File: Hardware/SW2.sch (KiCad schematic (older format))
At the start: 6 parts, among them SW2 SW_Rotary2x4

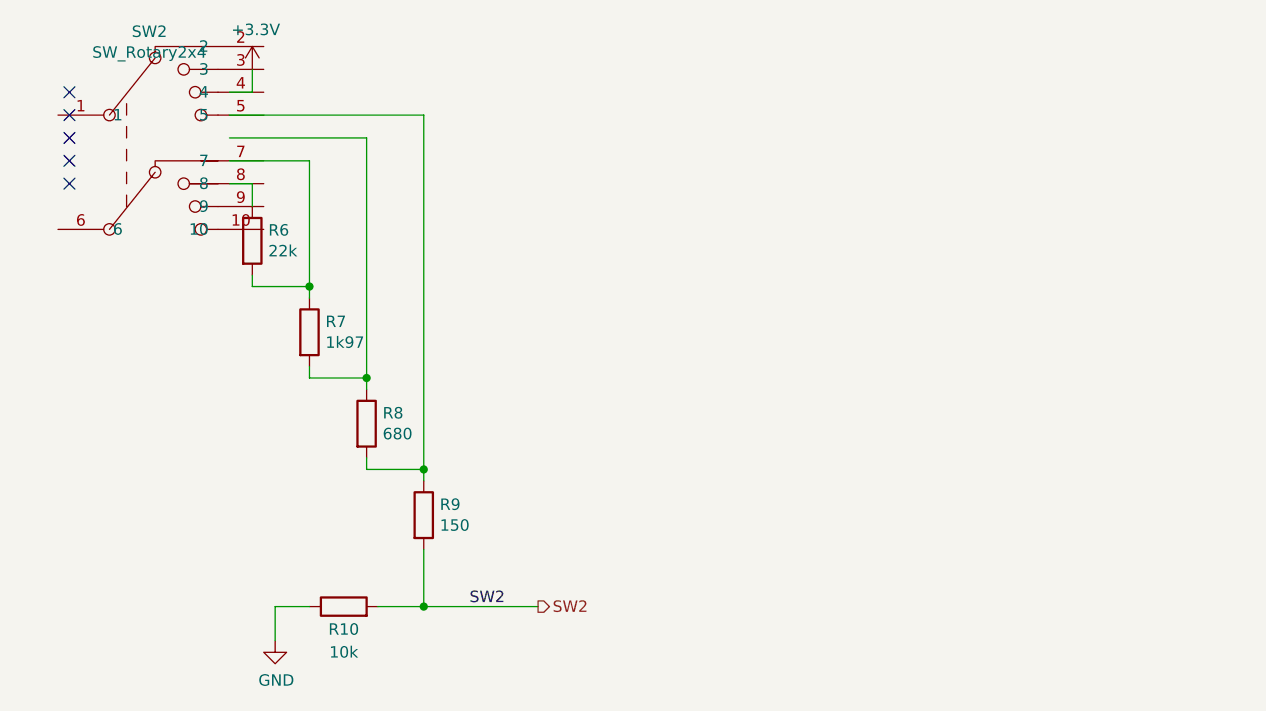
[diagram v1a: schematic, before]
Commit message: symbol changed, bigger cable hole in the middle
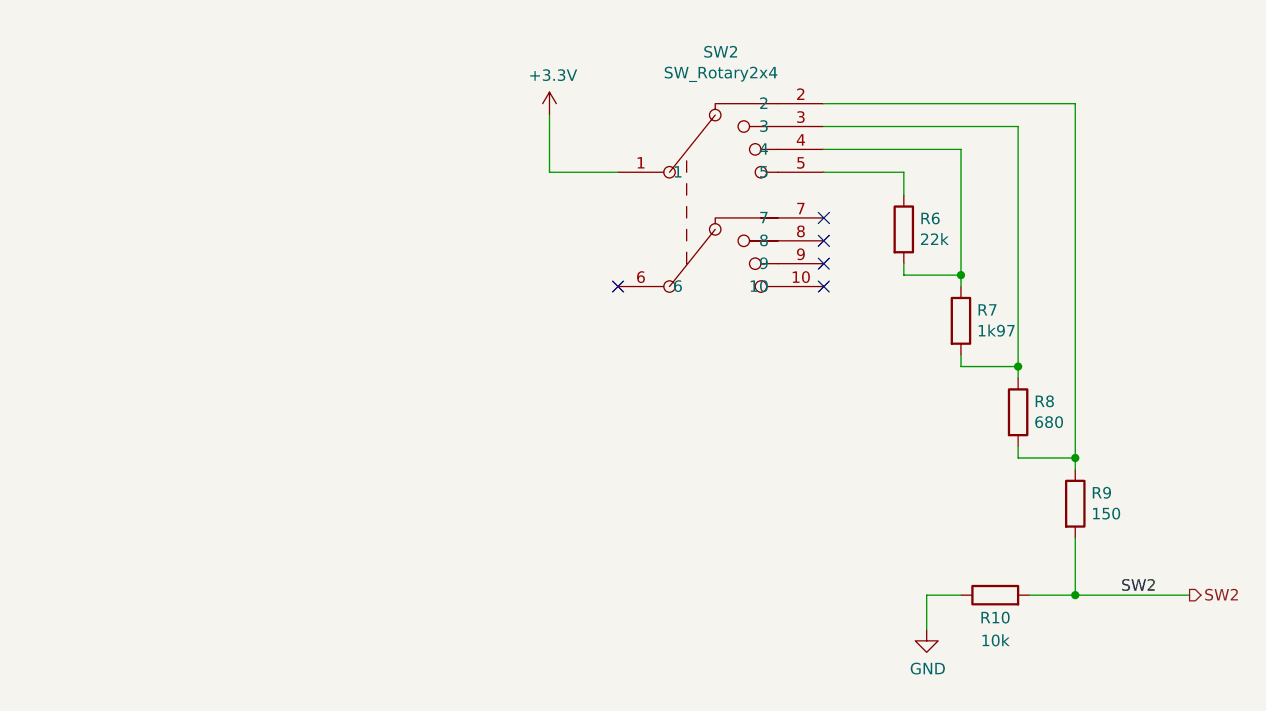
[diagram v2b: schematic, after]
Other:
- moved on the sheet: R10, R6, R7, R8, R9
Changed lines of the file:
@@
 $EndDescr
-$Comp
-L Switch:SW_Rotary2x4 SW?
-U 1 1 61B9B255
-P 4350 2700
-AR Path="/61B7E6EB/61B9B255" Ref="SW?"  Part="1"
-AR Path="/61B9708B/61B9B255" Ref="SW2"  Part="1"
-F 0 "SW2" H 4350 3115 50  0000 C CNN
-F 1 "SW_Rotary2x4" H 4350 3024 50  0000 C CNN
-F 2 "Rotary_Encoder:SW_Rotary2x4" H 4400 3150 50  0001 C CNN
-F 3 "https://www.piekarz.pl/21583-przelacznik-kh10-obrotowy-bistabilny-4xon-4-pozycje/" H 4400 3150 50  0001 C CNN
-	1    4350 2700
-	1    0    0    -1
-$EndComp
 $Comp
 L Device:R R?
 U 1 1 61B9B25B
-P 4800 3200
+P 7650 3150
 AR Path="/61B7E6EB/61B9B25B" Ref="R?"  Part="1"
 AR Path="/61B9708B/61B9B25B" Ref="R6"  Part="1"
-F 0 "R6" H 4870 3246 50  0000 L CNN
-F 1 "22k" H 4870 3155 50  0000 L CNN
-F 2 "Resistor_SMD:R_0603_1608Metric" V 4730 3200 50  0001 C CNN
-F 3 "~" H 4800 3200 50  0001 C CNN
-	1    4800 3200
+F 0 "R6" H 7720 3196 50  0000 L CNN
+F 1 "22k" H 7720 3105 50  0000 L CNN
+F 2 "Resistor_SMD:R_0603_1608Metric" V 7580 3150 50  0001 C CNN
+F 3 "~" H 7650 3150 50  0001 C CNN
+	1    7650 3150
 	1    0    0    -1
 $EndComp
@@
 L power:GND #PWR?
 U 1 1 61B9B261
-P 4900 4950
+P 7750 4900
 AR Path="/61B7E6EB/61B9B261" Ref="#PWR?"  Part="1"
 AR Path="/61B9708B/61B9B261" Ref="#PWR0103"  Part="1"
-F 0 "#PWR0103" H 4900 4700 50  0001 C CNN
-F 1 "GND" H 4905 4777 50  0000 C CNN
-F 2 "" H 4900 4950 50  0001 C CNN
-F 3 "" H 4900 4950 50  0001 C CNN
-	1    4900 4950
+F 0 "#PWR0103" H 7750 4650 50  0001 C CNN
+F 1 "GND" H 7755 4727 50  0000 C CNN
+F 2 "" H 7750 4900 50  0001 C CNN
+F 3 "" H 7750 4900 50  0001 C CNN
+	1    7750 4900
 	1    0    0    -1
 $EndComp
@@
 L power:+3.3V #PWR?
 U 1 1 61B9B267
-P 4800 2450
+P 6100 2650
 AR Path="/61B7E6EB/61B9B267" Ref="#PWR?"  Part="1"
 AR Path="/61B9708B/61B9B267" Ref="#PWR0104"  Part="1"
-F 0 "#PWR0104" H 4800 2300 50  0001 C CNN
-F 1 "+3.3V" H 4815 2623 50  0000 C CNN
-F 2 "" H 4800 2450 50  0001 C CNN
-F 3 "" H 4800 2450 50  0001 C CNN
-	1    4800 2450
+F 0 "#PWR0104" H 6100 2500 50  0001 C CNN
+F 1 "+3.3V" H 6115 2823 50  0000 C CNN
+F 2 "" H 6100 2650 50  0001 C CNN
+F 3 "" H 6100 2650 50  0001 C CNN
+	1    6100 2650
 	1    0    0    -1
 $EndComp
-Wire Wire Line
-	4800 2450 4800 2550
-Wire Wire Line
-	4800 2550 4700 2550
 $Comp
 L Device:R R?
 U 1 1 61B9B26F
-P 5050 3600
+P 7900 3550
 AR Path="/61B7E6EB/61B9B26F" Ref="R?"  Part="1"
 AR Path="/61B9708B/61B9B26F" Ref="R7"  Part="1"
-F 0 "R7" H 5120 3646 50  0000 L CNN
-F 1 "1k97" H 5120 3555 50  0000 L CNN
-F 2 "Resistor_SMD:R_0603_1608Metric" V 4980 3600 50  0001 C CNN
-F 3 "~" H 5050 3600 50  0001 C CNN
-	1    5050 3600
+F 0 "R7" H 7970 3596 50  0000 L CNN
+F 1 "1k97" H 7970 3505 50  0000 L CNN
+F 2 "Resistor_SMD:R_0603_1608Metric" V 7830 3550 50  0001 C CNN
+F 3 "~" H 7900 3550 50  0001 C CNN
+	1    7900 3550
 	1    0    0    -1
 $EndComp
@@
 L Device:R R?
 U 1 1 61B9B275
-P 5300 4000
+P 8150 3950
 AR Path="/61B7E6EB/61B9B275" Ref="R?"  Part="1"
 AR Path="/61B9708B/61B9B275" Ref="R8"  Part="1"
-F 0 "R8" H 5370 4046 50  0000 L CNN
-F 1 "680" H 5370 3955 50  0000 L CNN
-F 2 "Resistor_SMD:R_0603_1608Metric" V 5230 4000 50  0001 C CNN
-F 3 "~" H 5300 4000 50  0001 C CNN
-	1    5300 4000
+F 0 "R8" H 8220 3996 50  0000 L CNN
+F 1 "680" H 8220 3905 50  0000 L CNN
+F 2 "Resistor_SMD:R_0603_1608Metric" V 8080 3950 50  0001 C CNN
+F 3 "~" H 8150 3950 50  0001 C CNN
+	1    8150 3950
 	1    0    0    -1
 $EndComp
@@
 L Device:R R?
 U 1 1 61B9B27B
-P 5550 4400
+P 8400 4350
 AR Path="/61B7E6EB/61B9B27B" Ref="R?"  Part="1"
 AR Path="/61B9708B/61B9B27B" Ref="R9"  Part="1"
-F 0 "R9" H 5620 4446 50  0000 L CNN
-F 1 "150" H 5620 4355 50  0000 L CNN
-F 2 "Resistor_SMD:R_0603_1608Metric" V 5480 4400 50  0001 C CNN
-F 3 "~" H 5550 4400 50  0001 C CNN
-	1    5550 4400
+F 0 "R9" H 8470 4396 50  0000 L CNN
+F 1 "150" H 8470 4305 50  0000 L CNN
+F 2 "Resistor_SMD:R_0603_1608Metric" V 8330 4350 50  0001 C CNN
+F 3 "~" H 8400 4350 50  0001 C CNN
+	1    8400 4350
 	1    0    0    -1
 $EndComp
@@
 L Device:R R?
 U 1 1 61B9B281
-P 5200 4800
+P 8050 4750
 AR Path="/61B7E6EB/61B9B281" Ref="R?"  Part="1"
 AR Path="/61B9708B/61B9B281" Ref="R10"  Part="1"
-F 0 "R10" V 5100 4800 50  0000 C CNN
-F 1 "10k" V 5000 4800 50  0000 C CNN
-F 2 "Resistor_SMD:R_0603_1608Metric" V 5130 4800 50  0001 C CNN
-F 3 "~" H 5200 4800 50  0001 C CNN
-	1    5200 4800
+F 0 "R10" V 7950 4750 50  0000 C CNN
+F 1 "10k" V 7850 4750 50  0000 C CNN
+F 2 "Resistor_SMD:R_0603_1608Metric" V 7980 4750 50  0001 C CNN
+F 3 "~" H 8050 4750 50  0001 C CNN
+	1    8050 4750
 	0    -1   -1   0
 $EndComp
 Wire Wire Line
-	4900 4950 4900 4800
+	7750 4900 7750 4750
 Wire Wire Line
-	4900 4800 5050 4800
+	7750 4750 7900 4750
 Wire Wire Line
-	5350 4800 5550 4800
+	8200 4750 8400 4750
 Wire Wire Line
-	5550 4800 5550 4550
+	8400 4750 8400 4500
 Wire Wire Line
-	5550 4250 5550 4200
+	8400 4200 8400 4150
 Wire Wire Line
-	5550 4200 5300 4200
+	8400 4150 8150 4150
 Wire Wire Line
-	5300 4200 5300 4150
+	8150 4150 8150 4100
 Wire Wire Line
-	5300 3850 5300 3800
+	8150 3800 8150 3750
 Wire Wire Line
-	5300 3800 5050 3800
+	8150 3750 7900 3750
 Wire Wire Line
-	5050 3800 5050 3750
+	7900 3750 7900 3700
 Wire Wire Line
-	5050 3450 5050 3400
+	7900 3400 7900 3350
 Wire Wire Line
-	5050 3400 4800 3400
+	7900 3350 7650 3350
 Wire Wire Line
-	4800 3400 4800 3350
+	7650 3350 7650 3300
 Wire Wire Line
-	4800 3050 4800 2950
+	7650 3000 7650 2900
 Wire Wire Line
-	4800 2950 4700 2950
+	7900 3350 7900 2800
+Connection ~ 7900 3350
 Wire Wire Line
-	5050 3400 5050 2850
+	8150 2700 8150 3750
+Connection ~ 8150 3750
 Wire Wire Line
-	5050 2850 4700 2850
-Connection ~ 5050 3400
-Wire Wire Line
-	4700 2750 5300 2750
-Wire Wire Line
-	5300 2750 5300 3800
-Connection ~ 5300 3800
-Wire Wire Line
-	5550 4200 5550 2650
-Wire Wire Line
-	5550 2650 4700 2650
-Connection ~ 5550 4200
-Connection ~ 5550 4800
-Text Label 5750 4800 0    50   ~ 0
+	8400 4150 8400 2600
+Connection ~ 8400 4150
+Connection ~ 8400 4750
+Text Label 8600 4750 0    50   ~ 0
 SW2
-Text HLabel 6050 4800 2    50   Output ~ 0
+Text HLabel 8900 4750 2    50   Output ~ 0
 SW2
 Wire Wire Line
-	5550 4800 6050 4800
-NoConn ~ 4000 2550
-NoConn ~ 4000 2650
-NoConn ~ 4000 2750
-NoConn ~ 4000 2850
-NoConn ~ 4000 2950
+	8400 4750 8900 4750
+$Comp
+L Switch:SW_Rotary2x4 SW?
+U 1 1 61CDF86F
+P 6800 2950
+AR Path="/61B7E6EB/61CDF86F" Ref="SW?"  Part="1"
+AR Path="/61B9708B/61CDF86F" Ref="SW2"  Part="1"
+F 0 "SW2" H 6850 3525 50  0000 C CNN
+F 1 "SW_Rotary2x4" H 6850 3434 50  0000 C CNN
+F 2 "Rotary_Encoder:SW_Rotary2x4" H 6850 3600 50  0001 C CNN
+F 3 "https://www.piekarz.pl/21583-przelacznik-kh10-obrotowy-bistabilny-4xon-4-pozycje/" H 6850 3600 50  0001 C CNN
+	1    6800 2950
+	1    0    0    -1
+$EndComp
+Wire Wire Line
+	7300 2600 8400 2600
+Wire Wire Line
+	7300 2700 8150 2700
+Wire Wire Line
+	7300 2800 7900 2800
+Wire Wire Line
+	7300 2900 7650 2900
+Wire Wire Line
+	6100 2650 6100 2900
+Wire Wire Line
+	6100 2900 6400 2900
+NoConn ~ 7300 3100
+NoConn ~ 7300 3200
+NoConn ~ 7300 3300
+NoConn ~ 7300 3400
+NoConn ~ 6400 3400
 $EndSCHEMATC

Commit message: redesigned PCB
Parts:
- SW2: symbol Switch:SW_Rotary2x4 -> KieraV2-rescue:SW_Rotary2x4-Switch
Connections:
- net +3V3: now also SW2.13; no longer SW2.1
- net at R6.1: now also SW2.4; no longer SW2.5
- net at R6.2, R7.1: now also SW2.3; no longer SW2.4
- net at R7.2, R8.1: now also SW2.2; no longer SW2.3
- net at R8.2, R9.1: now also SW2.1; no longer SW2.2
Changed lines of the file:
@@
 	8400 4750 8900 4750
 $Comp
-L Switch:SW_Rotary2x4 SW?
+L KieraV2-rescue:SW_Rotary2x4-Switch SW?
 U 1 1 61CDF86F
 P 6800 2950
 AR Path="/61B7E6EB/61CDF86F" Ref="SW?"  Part="1"
 AR Path="/61B9708B/61CDF86F" Ref="SW2"  Part="1"
+AR Path="/61CDF86F" Ref="SW2"  Part="1"
 F 0 "SW2" H 6850 3525 50  0000 C CNN
 F 1 "SW_Rotary2x4" H 6850 3434 50  0000 C CNN

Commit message: wip
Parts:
- SW2: symbol KieraV2-rescue:SW_Rotary2x4-Switch -> Switch:SW_Rotary2x4
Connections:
- net +3V3: now also SW2.1; no longer SW2.13
- net at R6.1: now also SW2.5; no longer SW2.4
- net at R6.2, R7.1: now also SW2.4; no longer SW2.3
- net at R7.2, R8.1: now also SW2.3; no longer SW2.2
- net at R8.2, R9.1: now also SW2.2; no longer SW2.1
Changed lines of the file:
@@
 	8400 4750 8900 4750
 $Comp
-L KieraV2-rescue:SW_Rotary2x4-Switch SW?
+L Switch:SW_Rotary2x4 SW?
 U 1 1 61CDF86F
 P 6800 2950

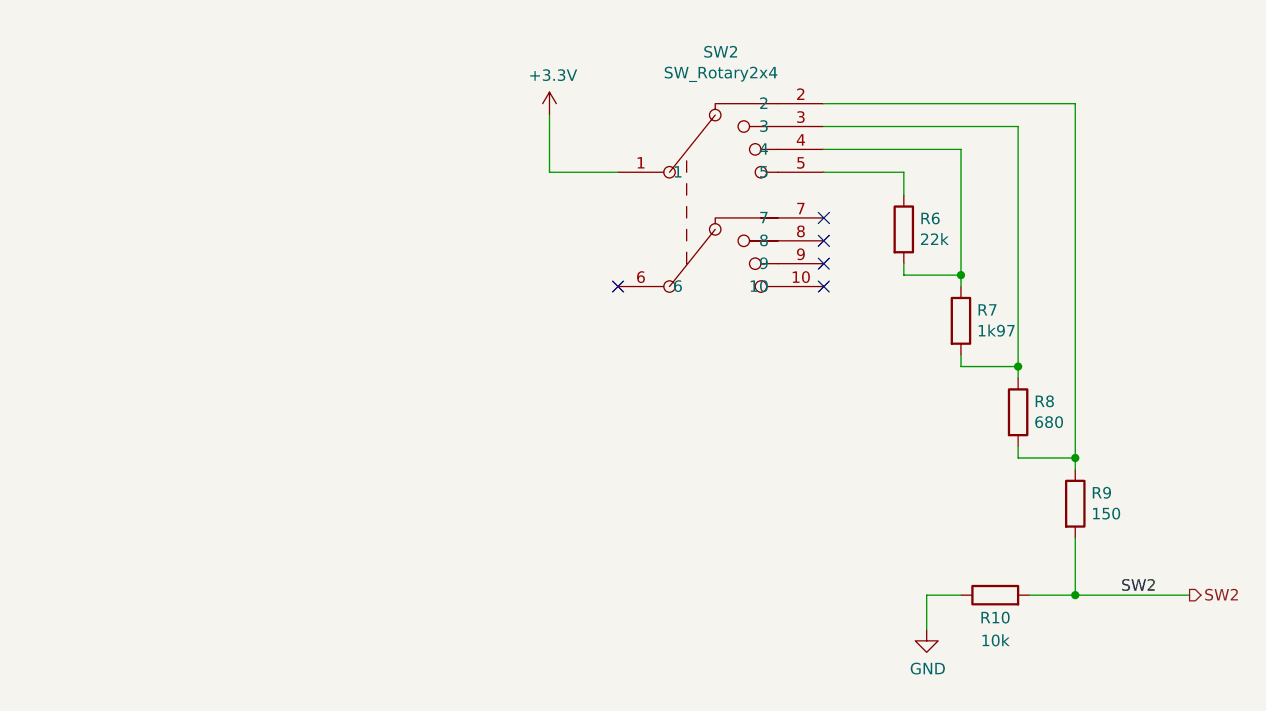
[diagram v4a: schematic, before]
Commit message: removed resistor ladder
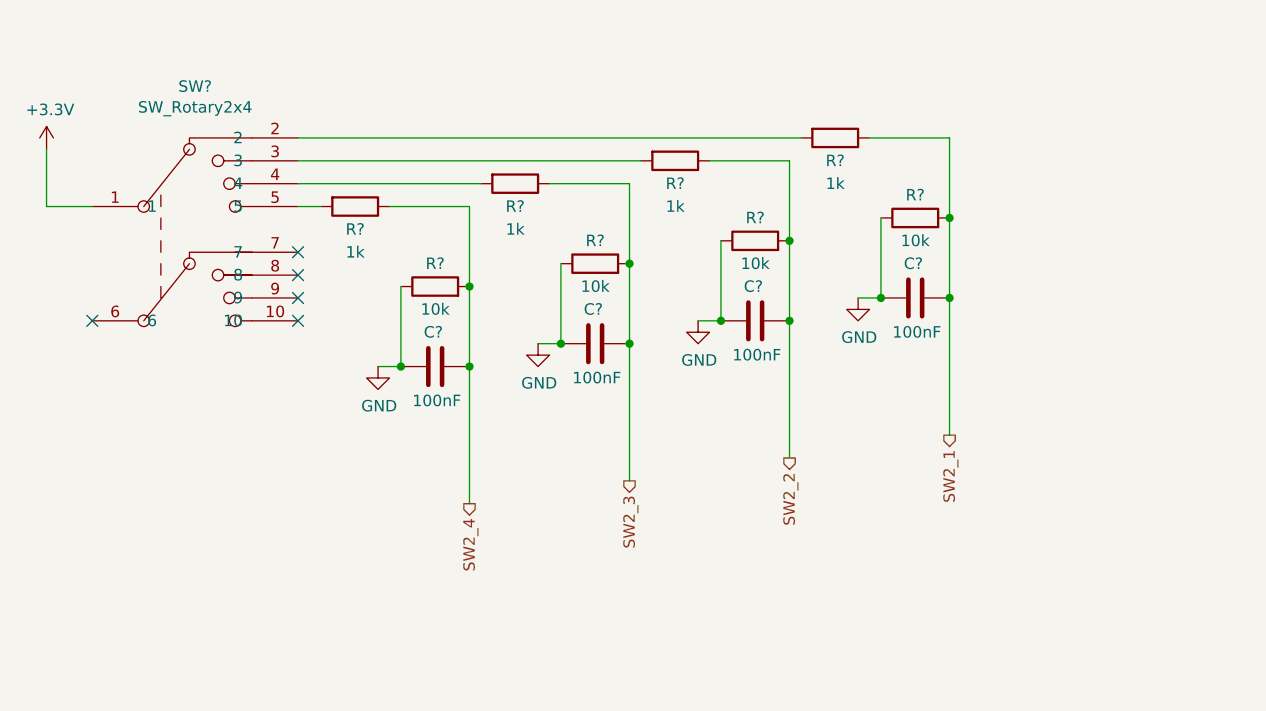
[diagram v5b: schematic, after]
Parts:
- removed R10: 10k, Resistor_SMD:R_0603_1608Metric, symbol Device:R
- removed R6: 22k, Resistor_SMD:R_0603_1608Metric, symbol Device:R
- removed R7: 1k97, Resistor_SMD:R_0603_1608Metric, symbol Device:R
- removed R8: 680, Resistor_SMD:R_0603_1608Metric, symbol Device:R
- removed R9: 150, Resistor_SMD:R_0603_1608Metric, symbol Device:R
- removed SW2: SW_Rotary2x4, Rotary_Encoder:SW_Rotary2x4, symbol Switch:SW_Rotary2x4
- added C? (x4): 100nF, Capacitor_SMD:C_0603_1608Metric, symbol Device:C
- added R? (x4): 10k, Resistor_SMD:R_0603_1608Metric, symbol Device:R
- added R? (x4): 1k, Resistor_SMD:R_0603_1608Metric, symbol Device:R
- added SW?: SW_Rotary2x4, Rotary_Encoder:SW_Rotary2x4, symbol Switch:SW_Rotary2x4
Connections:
- net +3V3: now also SW?.1
- net GND: now also C?.2, C?.2, C?.2, C?.2, R?.1, R?.1, R?.1, R?.1
- new net: R?.2, SW?.2
- new net: R?.2, SW?.3
- new net: R?.2, SW?.4
- new net: R?.2, SW?.5
- new net SW2_1: C?.1, R?.1, R?.2
- new net SW2_2: C?.1, R?.1, R?.2
- new net SW2_3: C?.1, R?.1, R?.2
- new net SW2_4: C?.1, R?.1, R?.2

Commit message: added more buttons
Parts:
- gave numbers to parts that had none: 13
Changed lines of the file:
@@
 AR Path="/629A99A3" Ref="SW?"  Part="1"
 AR Path="/61B7E6EB/629A99A3" Ref="SW?"  Part="1"
-F 0 "SW?" H 4550 3675 50  0000 C CNN
+AR Path="/61B9708B/629A99A3" Ref="SW2"  Part="1"
+F 0 "SW2" H 4550 3675 50  0000 C CNN
 F 1 "SW_Rotary2x4" H 4550 3584 50  0000 C CNN
 F 2 "Rotary_Encoder:SW_Rotary2x4" H 4550 3750 50  0001 C CNN
@@
 U 1 1 629A99A9
 P 3900 2800
-F 0 "#PWR?" H 3900 2650 50  0001 C CNN
+AR Path="/61B7E6EB/629A99A9" Ref="#PWR?"  Part="1"
+AR Path="/61B9708B/629A99A9" Ref="#PWR039"  Part="1"
+F 0 "#PWR039" H 3900 2650 50  0001 C CNN
 F 1 "+3.3V" H 3915 2973 50  0000 C CNN
 F 2 "" H 3900 2800 50  0001 C CNN
@@
 U 1 1 629A99AF
 P 5600 3400
-F 0 "R?" V 5700 3400 50  0000 C CNN
+AR Path="/61B9B4C0/629A99AF" Ref="R?"  Part="1"
+AR Path="/61B9708B/629A99AF" Ref="R10"  Part="1"
+F 0 "R10" V 5700 3400 50  0000 C CNN
 F 1 "10k" V 5500 3400 50  0000 C CNN
 F 2 "Resistor_SMD:R_0603_1608Metric" V 5530 3400 50  0001 C CNN
@@
 AR Path="/61B9B4C0/629A99B5" Ref="#PWR?"  Part="1"
 AR Path="/61B7E6EB/629A99B5" Ref="#PWR?"  Part="1"
-F 0 "#PWR?" H 5350 3500 50  0001 C CNN
+AR Path="/61B9708B/629A99B5" Ref="#PWR040"  Part="1"
+F 0 "#PWR040" H 5350 3500 50  0001 C CNN
 F 1 "GND" H 5355 3577 50  0000 C CNN
 F 2 "" H 5350 3750 50  0001 C CNN
@@
 U 1 1 629A99BE
 P 5250 3050
-F 0 "R?" V 5350 3050 50  0000 C CNN
+AR Path="/61B9B4C0/629A99BE" Ref="R?"  Part="1"
+AR Path="/61B9708B/629A99BE" Ref="R9"  Part="1"
+F 0 "R9" V 5350 3050 50  0000 C CNN
 F 1 "1k" V 5450 3050 50  0000 C CNN
 F 2 "Resistor_SMD:R_0603_1608Metric" V 5180 3050 50  0001 C CNN
@@
 U 1 1 629A99C4
 P 5600 3750
-F 0 "C?" V 5450 3700 50  0000 L CNN
+AR Path="/61B9B4C0/629A99C4" Ref="C?"  Part="1"
+AR Path="/61B9708B/629A99C4" Ref="C27"  Part="1"
+F 0 "C27" V 5450 3700 50  0000 L CNN
 F 1 "100nF" V 5750 3650 50  0000 L CNN
 F 2 "Capacitor_SMD:C_0603_1608Metric" H 5638 3600 50  0001 C CNN
@@
 U 1 1 629A99D2
 P 6300 3300
-F 0 "R?" V 6400 3300 50  0000 C CNN
+AR Path="/61B9B4C0/629A99D2" Ref="R?"  Part="1"
+AR Path="/61B9708B/629A99D2" Ref="R29"  Part="1"
+F 0 "R29" V 6400 3300 50  0000 C CNN
 F 1 "10k" V 6200 3300 50  0000 C CNN
 F 2 "Resistor_SMD:R_0603_1608Metric" V 6230 3300 50  0001 C CNN
@@
 AR Path="/61B9B4C0/629A99D8" Ref="#PWR?"  Part="1"
 AR Path="/61B7E6EB/629A99D8" Ref="#PWR?"  Part="1"
-F 0 "#PWR?" H 6050 3400 50  0001 C CNN
+AR Path="/61B9708B/629A99D8" Ref="#PWR041"  Part="1"
+F 0 "#PWR041" H 6050 3400 50  0001 C CNN
 F 1 "GND" H 6055 3477 50  0000 C CNN
 F 2 "" H 6050 3650 50  0001 C CNN
@@
 U 1 1 629A99E0
 P 5950 2950
-F 0 "R?" V 6050 2950 50  0000 C CNN
+AR Path="/61B9B4C0/629A99E0" Ref="R?"  Part="1"
+AR Path="/61B9708B/629A99E0" Ref="R28"  Part="1"
+F 0 "R28" V 6050 2950 50  0000 C CNN
 F 1 "1k" V 6150 2950 50  0000 C CNN
 F 2 "Resistor_SMD:R_0603_1608Metric" V 5880 2950 50  0001 C CNN
@@
 U 1 1 629A99E6
 P 6300 3650
-F 0 "C?" V 6150 3600 50  0000 L CNN
+AR Path="/61B9B4C0/629A99E6" Ref="C?"  Part="1"
+AR Path="/61B9708B/629A99E6" Ref="C28"  Part="1"
+F 0 "C28" V 6150 3600 50  0000 L CNN
 F 1 "100nF" V 6450 3550 50  0000 L CNN
 F 2 "Capacitor_SMD:C_0603_1608Metric" H 6338 3500 50  0001 C CNN
@@
 U 1 1 629A99F4
 P 7000 3200
-F 0 "R?" V 7100 3200 50  0000 C CNN
+AR Path="/61B9B4C0/629A99F4" Ref="R?"  Part="1"
+AR Path="/61B9708B/629A99F4" Ref="R31"  Part="1"
+F 0 "R31" V 7100 3200 50  0000 C CNN
 F 1 "10k" V 6900 3200 50  0000 C CNN
 F 2 "Resistor_SMD:R_0603_1608Metric" V 6930 3200 50  0001 C CNN
@@
 AR Path="/61B9B4C0/629A99FA" Ref="#PWR?"  Part="1"
 AR Path="/61B7E6EB/629A99FA" Ref="#PWR?"  Part="1"
-F 0 "#PWR?" H 6750 3300 50  0001 C CNN
+AR Path="/61B9708B/629A99FA" Ref="#PWR042"  Part="1"
+F 0 "#PWR042" H 6750 3300 50  0001 C CNN
 F 1 "GND" H 6755 3377 50  0000 C CNN
 F 2 "" H 6750 3550 50  0001 C CNN
@@
 U 1 1 629A9A02
 P 6650 2850
-F 0 "R?" V 6750 2850 50  0000 C CNN
+AR Path="/61B9B4C0/629A9A02" Ref="R?"  Part="1"
+AR Path="/61B9708B/629A9A02" Ref="R30"  Part="1"
+F 0 "R30" V 6750 2850 50  0000 C CNN
 F 1 "1k" V 6850 2850 50  0000 C CNN
 F 2 "Resistor_SMD:R_0603_1608Metric" V 6580 2850 50  0001 C CNN
@@
 U 1 1 629A9A08
 P 7000 3550
-F 0 "C?" V 6850 3500 50  0000 L CNN
+AR Path="/61B9B4C0/629A9A08" Ref="C?"  Part="1"
+AR Path="/61B9708B/629A9A08" Ref="C29"  Part="1"
+F 0 "C29" V 6850 3500 50  0000 L CNN
 F 1 "100nF" V 7150 3450 50  0000 L CNN
 F 2 "Capacitor_SMD:C_0603_1608Metric" H 7038 3400 50  0001 C CNN
@@
 U 1 1 629A9A16
 P 7700 3100
-F 0 "R?" V 7800 3100 50  0000 C CNN
+AR Path="/61B9B4C0/629A9A16" Ref="R?"  Part="1"
+AR Path="/61B9708B/629A9A16" Ref="R33"  Part="1"
+F 0 "R33" V 7800 3100 50  0000 C CNN
 F 1 "10k" V 7600 3100 50  0000 C CNN
 F 2 "Resistor_SMD:R_0603_1608Metric" V 7630 3100 50  0001 C CNN
@@
 AR Path="/61B9B4C0/629A9A1C" Ref="#PWR?"  Part="1"
 AR Path="/61B7E6EB/629A9A1C" Ref="#PWR?"  Part="1"
-F 0 "#PWR?" H 7450 3200 50  0001 C CNN
+AR Path="/61B9708B/629A9A1C" Ref="#PWR043"  Part="1"
+F 0 "#PWR043" H 7450 3200 50  0001 C CNN
 F 1 "GND" H 7455 3277 50  0000 C CNN
 F 2 "" H 7450 3450 50  0001 C CNN
@@
 U 1 1 629A9A24
 P 7350 2750
-F 0 "R?" V 7450 2750 50  0000 C CNN
+AR Path="/61B9B4C0/629A9A24" Ref="R?"  Part="1"
+AR Path="/61B9708B/629A9A24" Ref="R32"  Part="1"
+F 0 "R32" V 7450 2750 50  0000 C CNN
 F 1 "1k" V 7550 2750 50  0000 C CNN
 F 2 "Resistor_SMD:R_0603_1608Metric" V 7280 2750 50  0001 C CNN
@@
 U 1 1 629A9A2A
 P 7700 3450
-F 0 "C?" V 7550 3400 50  0000 L CNN
+AR Path="/61B9B4C0/629A9A2A" Ref="C?"  Part="1"
+AR Path="/61B9708B/629A9A2A" Ref="C30"  Part="1"
+F 0 "C30" V 7550 3400 50  0000 L CNN
 F 1 "100nF" V 7850 3350 50  0000 L CNN
 F 2 "Capacitor_SMD:C_0603_1608Metric" H 7738 3300 50  0001 C CNN
